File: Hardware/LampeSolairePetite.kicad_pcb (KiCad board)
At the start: 2 copper layers, 100 x 17.5 mm, 29 parts, among them J1 Connector, J2 CONN_ICSP, J3 Leds, J4 Led 2, P1 GREEN, P2 LED, P3 LED, P4 RED, P5 GREEN, U1 RF_RECEIVER, U2 PIC16F1827, U3 LD39200

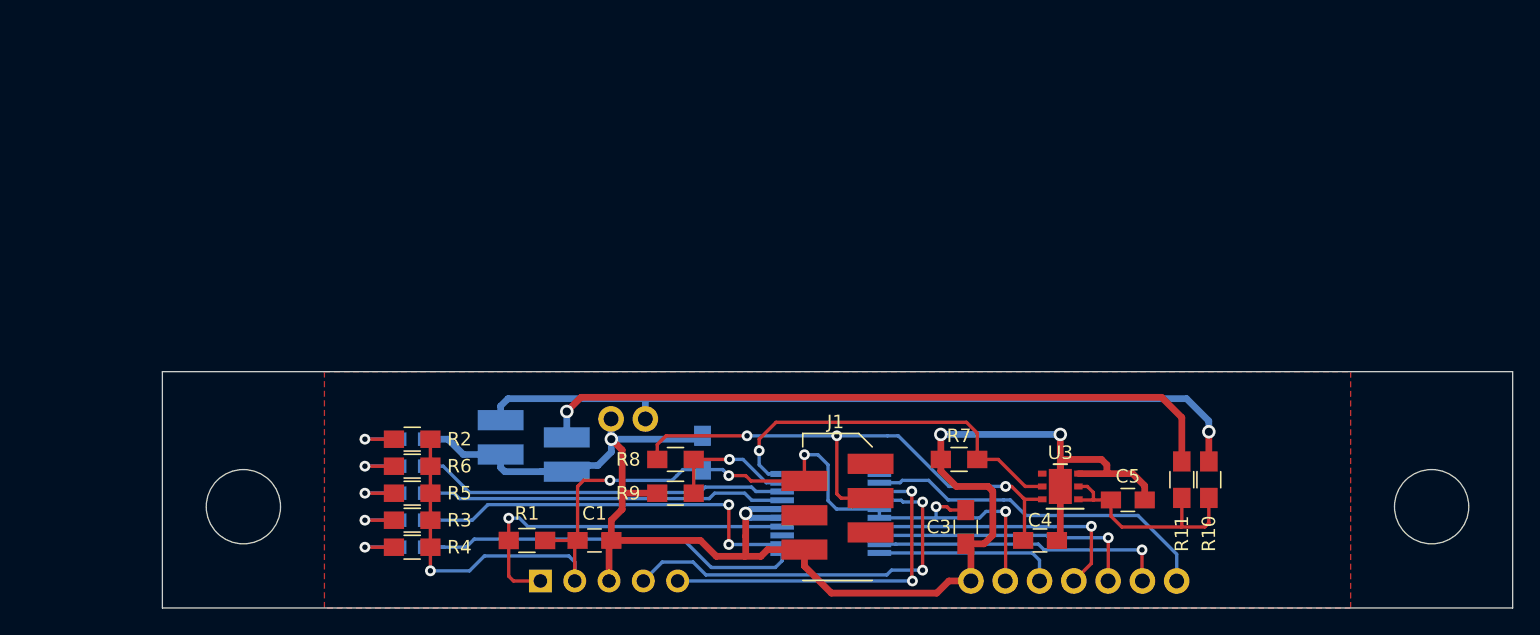
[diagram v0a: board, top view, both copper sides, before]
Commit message: PCB done for base card
Maybe add place for screws
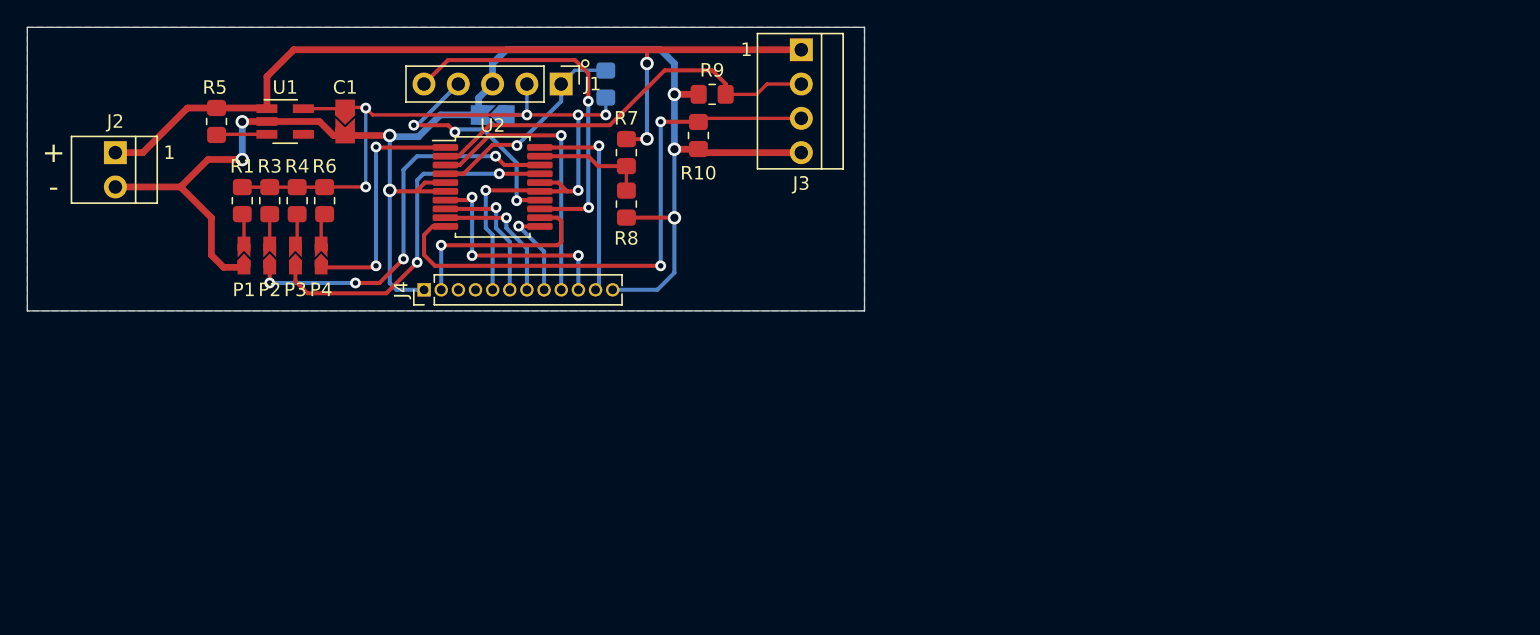
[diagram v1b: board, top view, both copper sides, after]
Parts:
- removed C3: 100nF, EsseivaN_Lib:C_0805_HandSoldering
- removed C4, C5: 4.7uF, EsseivaN_Lib:C_0805_HandSoldering
- removed P5: GREEN, EsseivaN_Lib:D_0603_HandSoldering
- removed R11: 10R, EsseivaN_Lib:R_0805_HandSoldering
- removed U3: LD39200, EsseivaN_Lib:DFN-6-1EP_3x3mm_Pitch0.95mm
- removed VIS_M3_88mm_space: ~, EsseivaN_Lib:VIS_M5_88mm
- C1: value 4.7uF -> 4.7 uF; footprint EsseivaN_Lib:C_0805_HandSoldering -> 0ESN_Lib:C_0805_2012Metric_Pad1.18x1.45mm_HandSolder
- C2: footprint EsseivaN_Lib:C_0805_HandSoldering -> 0ESN_Lib:C_0805_2012Metric_Pad1.18x1.45mm_HandSolder
- J1: value Connector -> CONN_ICSP; footprint EsseivaN_Lib:MicroMatch_6P_Female -> Connector_PinHeader_2.54mm:PinHeader_1x05_P2.54mm_Vertical
- J2: value CONN_ICSP -> Battery connector; footprint EsseivaN_Lib:Pin_Header_Straight_1x05_Pitch2.54mm -> 0ESN_Lib:Connector_2p_m; moved to F.Cu
- J3: value Leds -> Connector_4p_r; footprint EsseivaN_Lib:MicroMatch_4P_Female -> 0ESN_Lib:Connector_4p_m; moved to F.Cu
- J4: value Led 2 -> Connecteur LORA SX1278; footprint EsseivaN_Lib:WireConn_02 -> Connector_PinHeader_1.27mm:PinHeader_1x12_P1.27mm_Vertical; moved to F.Cu
- P1: footprint EsseivaN_Lib:D_0603_HandSoldering -> 0ESN_Lib:D_0603_1608Metric_Pad1.05x0.95mm_HandSolder; moved to F.Cu
- P2: value LED -> GREEN; footprint EsseivaN_Lib:D_0603_HandSoldering -> 0ESN_Lib:D_0603_1608Metric_Pad1.05x0.95mm_HandSolder; moved to F.Cu
- P3: value LED -> RED; footprint EsseivaN_Lib:D_0603_HandSoldering -> 0ESN_Lib:D_0603_1608Metric_Pad1.05x0.95mm_HandSolder; moved to F.Cu
- P4: value RED -> GREEN; footprint EsseivaN_Lib:D_0603_HandSoldering -> 0ESN_Lib:D_0603_1608Metric_Pad1.05x0.95mm_HandSolder; moved to F.Cu
- R1: value 27k -> 2k7; footprint EsseivaN_Lib:R_0805_HandSoldering -> Resistor_SMD:R_0805_2012Metric_Pad1.20x1.40mm_HandSolder
- R10: value 10R -> 4k7; footprint EsseivaN_Lib:R_0805_HandSoldering -> Resistor_SMD:R_0805_2012Metric_Pad1.20x1.40mm_HandSolder
- R2: value 1k5 -> 27k; footprint EsseivaN_Lib:R_0805_HandSoldering -> Resistor_SMD:R_0805_2012Metric_Pad1.20x1.40mm_HandSolder; moved to B.Cu
- R3: value 330R -> 2k7; footprint EsseivaN_Lib:R_0805_HandSoldering -> Resistor_SMD:R_0805_2012Metric_Pad1.20x1.40mm_HandSolder
- R4, R6: value 270R -> 2k7; footprint EsseivaN_Lib:R_0805_HandSoldering -> Resistor_SMD:R_0805_2012Metric_Pad1.20x1.40mm_HandSolder
- R5: value 330R -> 0R; footprint EsseivaN_Lib:R_0805_HandSoldering -> Resistor_SMD:R_0805_2012Metric_Pad1.20x1.40mm_HandSolder
- R7: value 4k7 -> 30k; footprint EsseivaN_Lib:R_0805_HandSoldering -> Resistor_SMD:R_0805_2012Metric_Pad1.20x1.40mm_HandSolder
- R8: value 30k -> 10k; footprint EsseivaN_Lib:R_0805_HandSoldering -> Resistor_SMD:R_0805_2012Metric_Pad1.20x1.40mm_HandSolder
- R9: value 10k -> 4k7; footprint EsseivaN_Lib:R_0805_HandSoldering -> Resistor_SMD:R_0805_2012Metric_Pad1.20x1.40mm_HandSolder
- U1: value RF_RECEIVER -> NCP114; footprint EsseivaN_Lib:RF_RECEIVER -> 0ESN_Lib:SOT-23-5_HandSoldering; moved to F.Cu
- U2: footprint EsseivaN_Lib:SSOP-20_5.3x7.2mm_Pitch0.65mm -> Package_SO:SSOP-20_5.3x7.2mm_P0.65mm; moved to F.Cu
- moved U1 67.6 mm to (109.1, 79.0)
- moved R10 45.6 mm to (139.7, 80.0), turned to -90 degrees
- moved J2 44.7 mm to (96.5, 81.3), turned to 0 degrees
- moved J1 37.4 mm to (129.5, 76.2)
- moved C1 36.1 mm to (113.5, 79.0), turned to -90 degrees
- moved J3 35.4 mm to (147.3, 73.7), turned to 0 degrees
- moved U2 34.8 mm to (124.5, 83.8)
- moved R7 33.5 mm to (134.4, 81.3), turned to -90 degrees
- moved R1 32.8 mm to (105.9, 84.8), turned to -90 degrees
- moved R5 31.1 mm to (104.0, 79.0), turned to -90 degrees
- moved R2 30.0 mm to (132.8, 76.2), turned to -90 degrees
- moved R9 29.7 mm to (140.7, 77.0)
- moved C2 29.4 mm to (124.5, 78.5), turned to 180 degrees
- moved R4 27.0 mm to (110.0, 84.8), turned to -90 degrees
- moved R3 25.9 mm to (108.0, 84.8), turned to -90 degrees
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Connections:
- J1 pad 1: Net-(J1-Pad1) -> MCLR
- J1 pad 3: VBAT -> GND
- J1 pad 4: Net-(J1-Pad4) -> ICSPDAT
- J1 pad 5: Net-(J1-Pad5) -> ICSPCLK
- J2 pad 1: /VPP -> VBAT
- J2 pad 2: VCC_3V3 -> GND
- J3 pad 1: Net-(J3-Pad1) -> VBAT
- J3 pad 2: Net-(J3-Pad2) -> ENABLE
- J3 pad 3: GND -> ENABLE_PWM
- J4 pad 1: Net-(J3-Pad1) -> GND
- J4 pad 2: GND -> DIO1
- P2 pad 1: /BATTERY_IND_R -> LED_GREEN
- P3 pad 1: /BATTERY_IND_G -> LED_RED
- P4 pad 1: /LED_G -> BATTERY_IND
- R1 pad 2: /VPP -> Net-(P1-Pad2)
- R10 pad 1: Net-(C5-Pad1) -> ENABLE_PWM
- R10 pad 2: Net-(J3-Pad1) -> GND
- R2 pad 1: VCC_3V3 -> MCLR
- R2 pad 2: Net-(P1-Pad2) -> VCC_3V3
- R5 pad 1: VCC_3V3 -> VBAT
- R5 pad 2: Net-(P4-Pad2) -> Net-(R5-Pad2)
- R6 pad 2: Net-(P5-Pad2) -> Net-(P4-Pad2)
- R7 pad 1: /ENABLE -> VBAT
- R7 pad 2: GND -> VBAT_MEAS
- R8 pad 1: VBAT -> VBAT_MEAS
- R8 pad 2: /BATTERY_LVL -> GND
- R9 pad 1: /BATTERY_LVL -> ENABLE
- U1 pad 1: GND -> VBAT
- U1 pad 2: VCC_3V3 -> GND
- U1 pad 3: /D0 -> Net-(R5-Pad2)
- U1 pad 4: /D1 -> unconnected-(U1-Pad4)
- U1 pad 5: /D2 -> VCC_3V3
- U2 pad 1: /BATTERY_IND_G -> BATTERY_IND
- U2 pad 10: /ENABLE -> ENABLE_PWM
- U2 pad 11: Net-(U2-Pad11) -> SCK
- U2 pad 12: /VT -> DIO1
- U2 pad 13: /ICSPCLK -> ICSPCLK
- U2 pad 14: /ICSPDAT -> ICSPDAT
- U2 pad 17: /D1 -> LED_RED
- U2 pad 18: /D2 -> LED_GREEN
- U2 pad 19: /D3 -> VBAT_MEAS
- U2 pad 2: /BATTERY_IND_R -> ENABLE
- U2 pad 20: /D0 -> REST
- U2 pad 3: Net-(U2-Pad3) -> NSS
- U2 pad 4: /VPP -> MCLR
- U2 pad 7: /LED_G -> DIO0
- U2 pad 8: /LED_R -> MISO
- U2 pad 9: /BATTERY_LVL -> MOSI
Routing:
- net Net-(J3-Pad1): track 58.9 -> 0.00 mm, vias 1 -> 0
- net Net-(J3-Pad2): track 51.8 -> 0.00 mm, vias 1 -> 0
- net ENABLE_PWM: track 0.00 -> 42.4 mm, vias 0 -> 2
- net ENABLE: track 0.00 -> 30.5 mm
- net /ICSPDAT: track 30.1 -> 0.00 mm, vias 2 -> 0
- net /BATTERY_IND_R: track 29.7 -> 0.00 mm, vias 2 -> 0
- net /BATTERY_IND_G: track 29.5 -> 0.00 mm
- net LED_GREEN: track 0.00 -> 29.2 mm, vias 0 -> 4
- net /ENABLE: track 28.5 -> 0.00 mm, vias 1 -> 0
- net /LED_R: track 27.4 -> 0.00 mm
- net /VPP: track 27.3 -> 0.00 mm, vias 1 -> 0
- net ICSPCLK: track 0.00 -> 26.9 mm, vias 0 -> 2
- net /LED_G: track 26.8 -> 0.00 mm
- net LED_RED: track 0.00 -> 26.7 mm, vias 0 -> 2
- net /ICSPCLK: track 26.5 -> 0.00 mm, vias 2 -> 0
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- added copper zone on B.Cu, net GND
- removed copper zone on F.Cu, net GND
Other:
- board size 100 x 17.5 mm -> 62 x 21 mm
- rule pad_to_mask_clearance: 0.05 -> 0
- board text added: "+"
- board text added: "LampeSolairePetite Esseiva Nicolas 2023.04.02 - R10"
- board text removed: "B0"
- board text removed: "B1"
- board text removed: "ICSP"
- board text removed: "Ind0"
- board text removed: "Ind1"
- board text removed: "LampeSolaire 2 Esseiva Nicolas 26092020 - R00"
- board text removed: "Power"

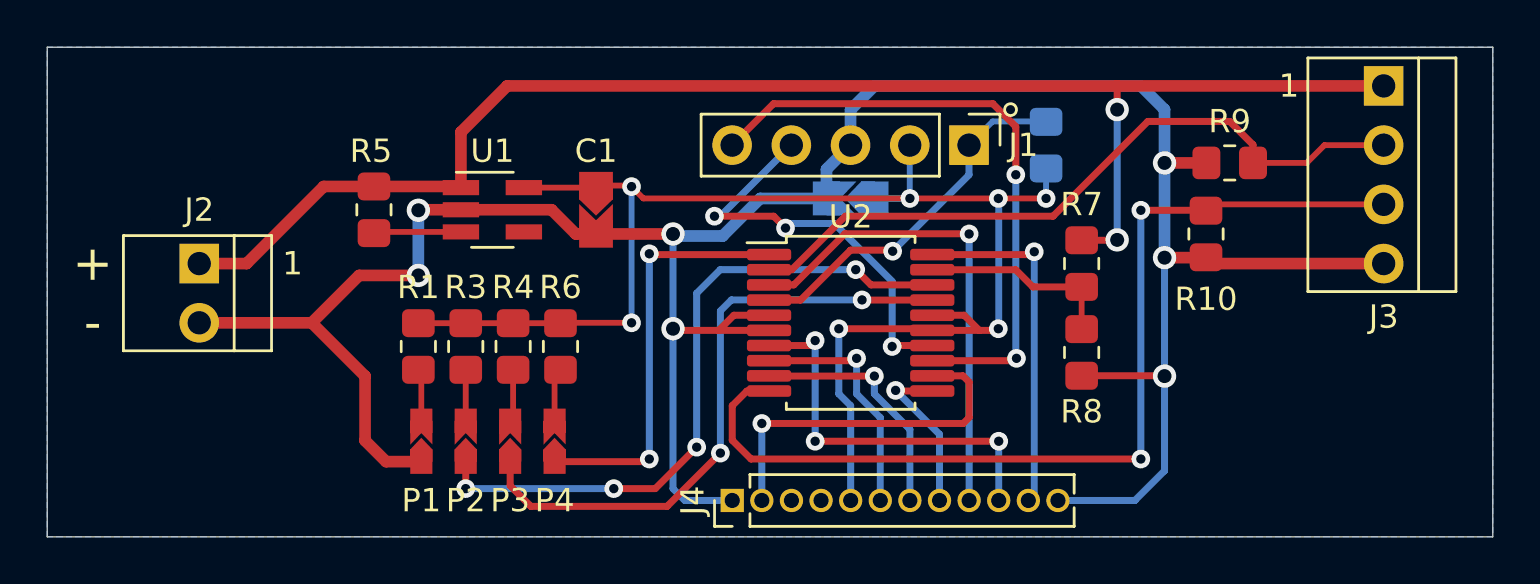
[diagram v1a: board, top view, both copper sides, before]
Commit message: Added holes
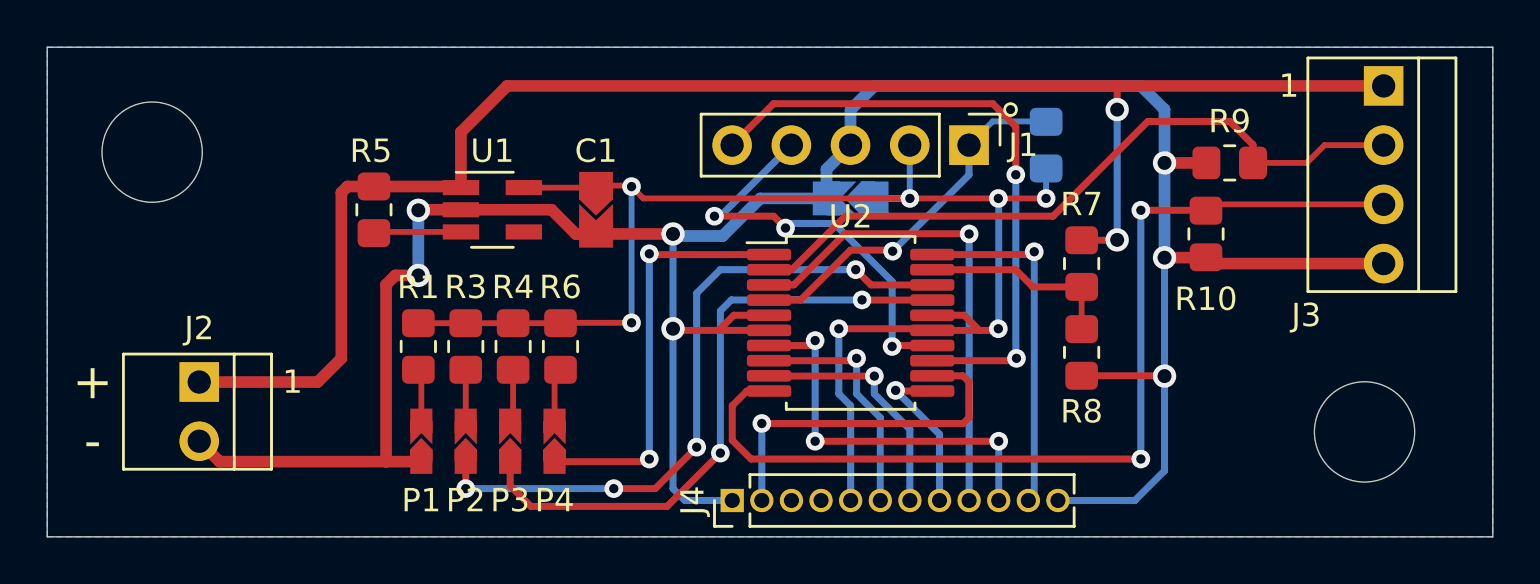
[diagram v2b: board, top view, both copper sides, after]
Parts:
- added REF**: MountingHole_4.3mm_M4, MountingHole:MountingHole_4.3mm_M4, F.Cu at (146.5, 88.5)
- added REF**: MountingHole_4.3mm_M4, MountingHole:MountingHole_4.3mm_M4, F.Cu at (94.5, 76.5)
- moved J2 5.08 mm to (96.5, 86.4)
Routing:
- net VBAT: track 63.5 -> 69.8 mm
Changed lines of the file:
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@@
       (svgprecision 6)
       (excludeedgelayer false)
-      (plotframeref true)
+      (plotframeref false)
       (viasonmask false)
       (mode 1)
@@
       (psnegative false)
       (psa4output false)
-      (plotreference true)
+      (plotreference false)
       (plotvalue true)
       (plotinvisibletext false)
       (sketchpadsonfab false)
       (subtractmaskfromsilk false)
-      (outputformat 4)
+      (outputformat 1)
       (mirror false)
       (drillshape 0)
       (scaleselection 1)
-      (outputdirectory "../Fabrication/PDF")
+      (outputdirectory "../Fabrication/Gerber")
     )
   )
@@
   )
   (footprint "0ESN_Lib:Connector_2p_m" (layer "F.Cu")
-    (at 96.52 81.28)
+    (at 96.52 86.36)
     (descr "Through hole straight pin header, 1x06, 2.54mm pitch, single row")
     (tags "Through hole pin header THT 1x06 2.54mm single row")
@@
       (rotate (xyz -90 0 90))
     )
+  )
+  (footprint "MountingHole:MountingHole_4.3mm_M4" locked (layer "F.Cu")
+    (at 146.5 88.5)
+    (descr "Mounting Hole 4.3mm, no annular, M4")
+    (tags "mounting hole 4.3mm no annular m4")
+    (attr exclude_from_pos_files exclude_from_bom)
+    (fp_text reference "REF**" (at 0 -5.3) (layer "F.SilkS") hide
+      (effects (font (size 1 1) (thickness 0.15)))
+    )
+    (fp_text value "MountingHole_4.3mm_M4" (at 0 5.3) (layer "F.Fab")
+      (effects (font (size 1 1) (thickness 0.15)))
+    )
+    (fp_text user "${REFERENCE}" (at 0 0) (layer "F.Fab")
+      (effects (font (size 1 1) (thickness 0.15)))
+    )
+    (fp_circle (center 0 0) (end 4.3 0) (layer "Cmts.User") (width 0.15) (fill none))
+    (fp_circle (center 0 0) (end 4.55 0) (layer "F.CrtYd") (width 0.05) (fill none))
+    (pad "" np_thru_hole circle locked (at 0 0) (size 4.3 4.3) (drill 4.3) (layers *.Cu *.Mask))
   )
   (footprint "0ESN_Lib:SOT-23-5_HandSoldering" (layer "F.Cu")
@@
       (rotate (xyz 0 0 0))
     )
+  )
+  (footprint "MountingHole:MountingHole_4.3mm_M4" locked (layer "F.Cu")
+    (at 94.5 76.5)
+    (descr "Mounting Hole 4.3mm, no annular, M4")
+    (tags "mounting hole 4.3mm no annular m4")
+    (attr exclude_from_pos_files exclude_from_bom)
+    (fp_text reference "REF**" (at 0 -5.3) (layer "F.SilkS") hide
+      (effects (font (size 1 1) (thickness 0.15)))
+    )
+    (fp_text value "MountingHole_4.3mm_M4" (at 0 5.3) (layer "F.Fab")
+      (effects (font (size 1 1) (thickness 0.15)))
+    )
+    (fp_text user "${REFERENCE}" (at 0 0) (layer "F.Fab")
+      (effects (font (size 1 1) (thickness 0.15)))
+    )
+    (fp_circle (center 0 0) (end 4.3 0) (layer "Cmts.User") (width 0.15) (fill none))
+    (fp_circle (center 0 0) (end 4.55 0) (layer "F.CrtYd") (width 0.05) (fill none))
+    (pad "" np_thru_hole circle locked (at 0 0) (size 4.3 4.3) (drill 4.3) (layers *.Cu *.Mask))
   )
   (footprint "0ESN_Lib:C_0805_2012Metric_Pad1.18x1.45mm_HandSolder" (layer "F.Cu")
@@
     (property "Sheetname" "")
     (attr through_hole)
-    (fp_text reference "J3" (at 0 9.906) (layer "F.SilkS")
+    (fp_text reference "J3" (at -3.32 9.84) (layer "F.SilkS")
       (effects (font (size 1 1) (thickness 0.15)))
     )
@@
     (effects (font (size 1 1) (thickness 0.2)) (justify mirror))
   )
-  (gr_text "+" (at 91.948 81.28) (layer "F.SilkS")
+  (gr_text "+" (at 91.948 86.36) (layer "F.SilkS")
     (effects (font (size 1.5 1.5) (thickness 0.3)))
   )
-  (gr_text "-" (at 91.948 83.82) (layer "F.SilkS")
+  (gr_text "-" (at 91.948 88.9) (layer "F.SilkS")
     (effects (font (size 1.5 1.5) (thickness 0.3)))
   )
@@
   (segment (start 107.743 78.9725) (end 105.9395 78.9725) (width 0.5) (layer "F.Cu") (net 1))
   (segment (start 113.538 80.01) (end 116.84 80.01) (width 0.5) (layer "F.Cu") (net 1))
-  (segment (start 101.346 83.82) (end 96.52 83.82) (width 0.5) (layer "F.Cu") (net 1))
+  (segment (start 104.535 89.775) (end 106.045 89.775) (width 0.5) (layer "F.Cu") (net 1))
   (segment (start 112.6705 80.01) (end 113.538 80.01) (width 0.5) (layer "F.Cu") (net 1))
   (segment (start 134.366 86.09) (end 137.906 86.09) (width 0.3) (layer "F.Cu") (net 1))
+  (segment (start 97.395 89.775) (end 104.535 89.775) (width 0.5) (layer "F.Cu") (net 1))
   (segment (start 147.32 81.28) (end 139.97 81.28) (width 0.5) (layer "F.Cu") (net 1))
   (segment (start 139.716 76.962) (end 137.922 76.962) (width 0.5) (layer "F.Cu") (net 1))
   (segment (start 120.96 84.145) (end 118.801 84.145) (width 0.3) (layer "F.Cu") (net 1))
-  (segment (start 103.632 86.106) (end 103.632 88.872) (width 0.5) (layer "F.Cu") (net 1))
-  (segment (start 105.918 81.788) (end 103.378 81.788) (width 0.5) (layer "F.Cu") (net 1))
   (segment (start 137.906 86.09) (end 137.922 86.106) (width 0.3) (layer "F.Cu") (net 1))
   (segment (start 118.801 84.145) (end 116.911 84.145) (width 0.3) (layer "F.Cu") (net 1))
+  (segment (start 104.93 81.788) (end 104.535 82.183) (width 0.5) (layer "F.Cu") (net 1))
   (segment (start 139.97 81.28) (end 139.7 81.01) (width 0.5) (layer "F.Cu") (net 1))
   (segment (start 105.9395 78.9725) (end 105.918 78.994) (width 0.5) (layer "F.Cu") (net 1))
-  (segment (start 101.346 83.82) (end 103.632 86.106) (width 0.5) (layer "F.Cu") (net 1))
   (segment (start 119.451 83.495) (end 118.801 84.145) (width 0.3) (layer "F.Cu") (net 1))
   (segment (start 137.922 81.026) (end 139.684 81.026) (width 0.5) (layer "F.Cu") (net 1))
   (segment (start 120.96 83.495) (end 119.451 83.495) (width 0.3) (layer "F.Cu") (net 1))
-  (segment (start 103.378 81.788) (end 101.346 83.82) (width 0.5) (layer "F.Cu") (net 1))
+  (segment (start 96.52 88.9) (end 97.395 89.775) (width 0.5) (layer "F.Cu") (net 1))
   (segment (start 116.911 84.145) (end 116.84 84.074) (width 0.3) (layer "F.Cu") (net 1))
-  (segment (start 103.632 88.872) (end 104.535 89.775) (width 0.5) (layer "F.Cu") (net 1))
+  (segment (start 105.918 81.788) (end 104.93 81.788) (width 0.5) (layer "F.Cu") (net 1))
+  (segment (start 104.535 82.183) (end 104.535 89.775) (width 0.5) (layer "F.Cu") (net 1))
   (segment (start 107.743 78.9725) (end 111.633 78.9725) (width 0.5) (layer "F.Cu") (net 1))
   (segment (start 139.684 81.026) (end 139.7 81.01) (width 0.5) (layer "F.Cu") (net 1))
-  (segment (start 106.045 89.775) (end 104.535 89.775) (width 0.5) (layer "F.Cu") (net 1))
   (via (at 137.922 76.962) (size 1) (drill 0.6) (layers "F.Cu" "B.Cu") (net 1))
   (via (at 116.84 84.074) (size 1) (drill 0.6) (layers "F.Cu" "B.Cu") (net 1))
@@
   (segment (start 124.46 87.376) (end 123.952 86.868) (width 0.3) (layer "B.Cu") (net 2))
   (segment (start 135.874 80.28) (end 135.89 80.264) (width 0.3) (layer "F.Cu") (net 3))
+  (segment (start 102.616 78.232) (end 102.616 85.344) (width 0.5) (layer "F.Cu") (net 3))
   (segment (start 135.89 74.676) (end 135.89 73.66) (width 0.3) (layer "F.Cu") (net 3))
+  (segment (start 102.8755 77.9725) (end 102.616 78.232) (width 0.5) (layer "F.Cu") (net 3))
+  (segment (start 104.013 77.9725) (end 102.8755 77.9725) (width 0.5) (layer "F.Cu") (net 3))
   (segment (start 134.366 80.28) (end 135.874 80.28) (width 0.3) (layer "F.Cu") (net 3))
   (segment (start 107.743 75.645) (end 109.728 73.66) (width 0.5) (layer "F.Cu") (net 3))
+  (segment (start 101.6 86.36) (end 96.52 86.36) (width 0.5) (layer "F.Cu") (net 3))
   (segment (start 107.743 78.0225) (end 107.743 75.645) (width 0.5) (layer "F.Cu") (net 3))
   (segment (start 109.728 73.66) (end 135.89 73.66) (width 0.5) (layer "F.Cu") (net 3))
   (segment (start 104.013 77.9725) (end 107.693 77.9725) (width 0.5) (layer "F.Cu") (net 3))
   (segment (start 107.693 77.9725) (end 107.743 78.0225) (width 0.5) (layer "F.Cu") (net 3))
-  (segment (start 96.52 81.28) (end 98.552 81.28) (width 0.5) (layer "F.Cu") (net 3))
-  (segment (start 101.8595 77.9725) (end 104.013 77.9725) (width 0.5) (layer "F.Cu") (net 3))
+  (segment (start 102.616 85.344) (end 101.6 86.36) (width 0.5) (layer "F.Cu") (net 3))
   (segment (start 135.89 73.66) (end 147.32 73.66) (width 0.5) (layer "F.Cu") (net 3))
-  (segment (start 98.552 81.28) (end 101.8595 77.9725) (width 0.5) (layer "F.Cu") (net 3))
   (via (at 135.89 80.264) (size 1) (drill 0.6) (layers "F.Cu" "B.Cu") (net 3))
   (via (at 135.89 74.676) (size 1) (drill 0.6) (layers "F.Cu" "B.Cu") (net 3))
